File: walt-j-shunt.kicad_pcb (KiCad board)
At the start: 2 copper layers, 39 parts, among them Q1 NMOS, Q2 PNP, Q3 PNP

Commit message: basic layout positive
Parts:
- C1, C2: footprint Capacitor_THT:CP_Radial_D18.0mm_P7.50mm -> Capacitor_THT:CP_Radial_D12.5mm_P5.00mm
- C3: footprint Capacitor_THT:CP_Radial_D18.0mm_P7.50mm -> Samacsys:B32529C105J
- C4: footprint Capacitor_THT:CP_Radial_D5.0mm_P2.00mm -> Capacitor_SMD:C_0805_2012Metric
- D1, D2, D3, D4: footprint Diode_SMD:D_SMC -> Diode_SMD:D_SOD-123
- D6, D7: footprint Diode_SMD:D_SMC -> Diode_SMD:D_SOD-123F
- Q1: footprint Package_TO_SOT_THT:TO-3P-3_Horizontal_TabDown -> Package_TO_SOT_THT:TO-220-3_Horizontal_TabDown
- Q2: footprint Package_TO_SOT_THT:TO-3P-3_Horizontal_TabDown -> Package_TO_SOT_SMD:TO-252-2
- Q3: footprint Package_TO_SOT_THT:TO-3P-3_Horizontal_TabDown -> Package_TO_SOT_SMD:SOT-23-3
- R10, R9: footprint Resistor_SMD:R_1206_3216Metric -> Resistor_SMD:R_MELF_MMB-0207
- U1: value ~ -> AD817; footprint Package_SO:SOIC-8-1EP_3.9x4.9mm_P1.27mm_EP2.41x3.3mm -> Package_SO:SOIC-8_3.9x4.9mm_P1.27mm
- V1: value VSIN -> VPULSE
- moved H2 79.3 mm to (52.5, 90.0)
- moved H1 77.8 mm to (50.0, 52.5)
- moved V1 63.8 mm to (78.2, 70.5), turned to 90 degrees
- moved H3 57.8 mm to (170.0, 32.5)
- moved R1 53.9 mm to (88.0, 70.0), turned to 180 degrees
- moved D1 44.2 mm to (80.0, 79.0), turned to 180 degrees
- moved R2 43.6 mm to (99.0, 72.0), turned to 90 degrees
- moved R3 43.2 mm to (107.0, 61.0)
- moved R4 42.7 mm to (107.0, 65.0)
- moved D9 41.6 mm to (122.0, 64.7), turned to -90 degrees
- moved D2 40.0 mm to (80.0, 76.0)
- moved C1 39.8 mm to (92.0, 75.7), turned to -90 degrees
- moved D3 39.6 mm to (80.0, 82.0), turned to 180 degrees
- moved D4 38.8 mm to (80.0, 85.0)
- moved H4 36.1 mm to (160.0, 95.0)
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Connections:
- net Net-(Q1-D) renamed pre-cur
- U1 pad 1: Net-(D6-A) -> unconnected-(U1-NULL-Pad1)
- U1 pad 3: out -> Net-(D6-A)
- U1 pad 5: Net-(D5-K) -> unconnected-(U1-NC-Pad5)
- U1 pad 6: (no net) -> Net-(D5-K)
- U1 pad 7: (no net) -> out
- U1 pad 8: (no net) -> unconnected-(U1-NULL-Pad8)
- V1 pad 1: Net-(D1-A) -> ac
- V1 pad 2: ac -> Net-(D1-A)
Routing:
- net out: track 0.00 -> 106.4 mm
- net Net-(D6-A): track 0.00 -> 26.0 mm
- net Net-(D6-K): track 0.00 -> 25.7 mm
- net Net-(U1--): track 0.00 -> 16.9 mm
- net vref: track 0.00 -> 14.0 mm
- net Net-(D5-K): track 0.00 -> 13.0 mm
- net Net-(Q2-B): track 0.00 -> 12.7 mm
- net Net-(Q2-E): track 0.00 -> 12.3 mm
- net Net-(D5-A): track 0.00 -> 7.67 mm
- net Net-(D8-K): track 0.00 -> 4.80 mm

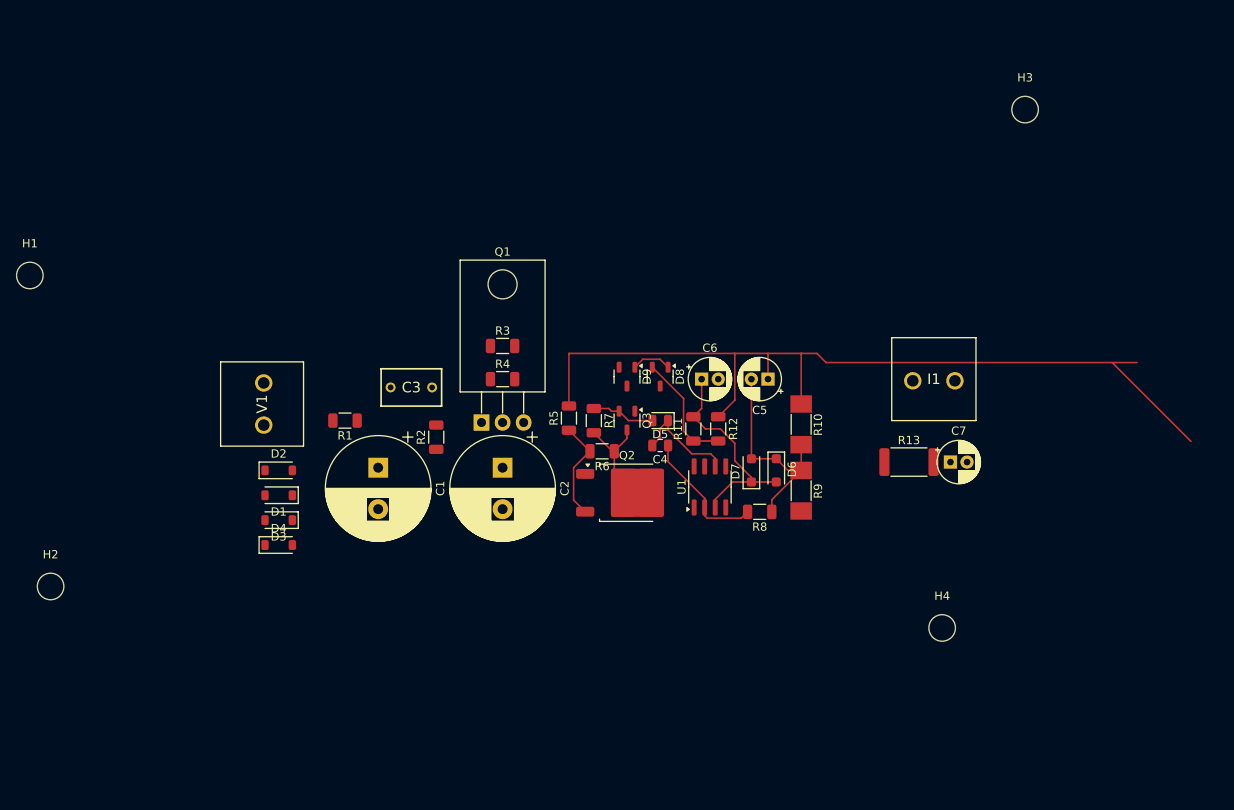
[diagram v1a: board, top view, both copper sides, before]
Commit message: plus only, cap and rectififer on board
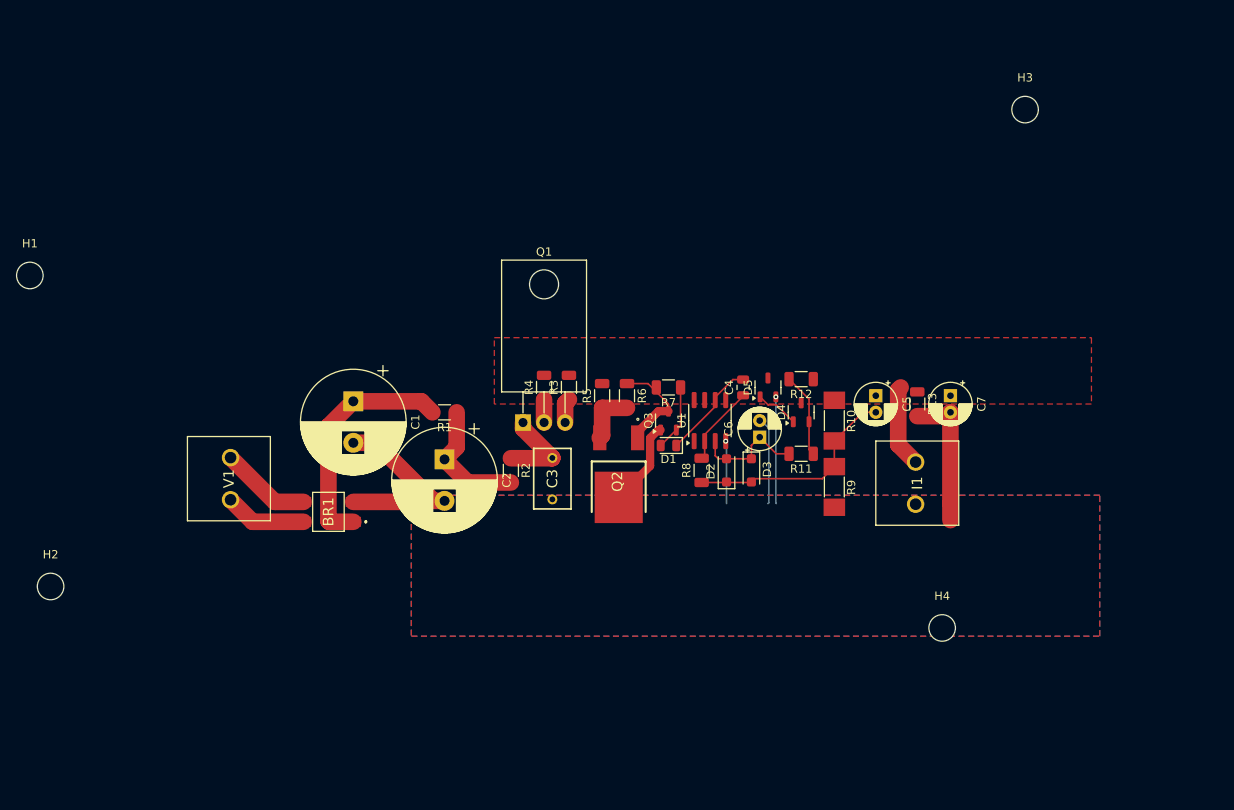
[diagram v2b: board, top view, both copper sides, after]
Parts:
- removed the D1 at (80.0, 79.0)
- removed the D2 at (80.0, 76.0)
- removed the D3 at (80.0, 82.0)
- removed the D4 at (80.0, 85.0)
- added BR1: CDBHM140L-G, Samacsys:CDBHM140LG, F.Cu at (86.0, 81.0)
- Q2: value PNP -> NJVMJD45H11T4G; footprint Package_TO_SOT_SMD:TO-252-2 -> Samacsys:DPAK_(SINGLE-GAUGE)_TO-252(369C)_ISSUE_F
- R13: footprint Resistor_SMD:R_2512_6332Metric -> Resistor_SMD:R_1206_3216Metric
- moved C3 21.3 mm to (113.0, 74.5), turned to -90 degrees
- moved D4 17.5 mm to (143.0, 69.0), turned to 90 degrees
- moved D5 17.0 mm to (139.0, 66.0), turned to 90 degrees
- moved R11 13.3 mm to (143.0, 74.0), turned to 180 degrees
- moved C5 13.2 mm to (152.0, 67.0), turned to -90 degrees
- moved C4 12.2 mm to (136.0, 66.0), turned to 90 degrees
- moved R1 12.0 mm to (100.0, 69.0)
- moved R12 11.7 mm to (143.0, 65.0), turned to 180 degrees
- moved C6 9.90 mm to (138.0, 72.0), turned to 90 degrees
- moved R2 9.85 mm to (108.0, 76.0), turned to -90 degrees
- moved R7 9.85 mm to (127.0, 66.0), turned to 180 degrees
- moved V1 9.85 mm to (74.2, 79.5)
- moved I1 9.81 mm to (156.8, 75.0), turned to -90 degrees
- moved R3 9.43 mm to (115.0, 66.0), turned to 90 degrees
- moved R8 8.60 mm to (131.0, 76.0), turned to 90 degrees
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- renumbered D5 to D1, D6 to D2, D7 to D3, D8 to D4, D9 to D5
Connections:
- Q2 pad 1: GND -> Net-(Q3-E)
- Q2 pad 2: Net-(Q2-B) -> Net-(Q2-Pad2)
- Q2 pad 3: Net-(Q2-E) -> GND
- Q3 pad 3: Net-(Q2-B) -> Net-(Q3-E)
- R5 pad 1: Net-(Q2-E) -> Net-(Q2-Pad2)
- R6 pad 1: Net-(Q2-B) -> Net-(Q3-E)
- R6 pad 2: Net-(Q2-E) -> Net-(Q2-Pad2)
- R7 pad 2: Net-(Q2-B) -> Net-(Q3-E)
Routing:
- net out: track 106.4 -> 9.99 mm
- net GND: track 0.00 -> 83.5 mm, vias 0 -> 2
- net Net-(BR1-+): track 0.00 -> 28.8 mm
- net Net-(C2-Pad1): track 0.00 -> 15.4 mm
- net Net-(Q2-B): track 12.7 -> 0.00 mm
- net Net-(Q3-E): track 0.00 -> 12.3 mm
- net Net-(Q2-E): track 12.3 -> 0.00 mm
- net Net-(D2-A): track 26.0 -> 13.8 mm
- net Net-(BR1-~{_2}): track 0.00 -> 11.0 mm
- net pre-cur: track 0.00 -> 10.8 mm
- net ac: track 0.00 -> 9.90 mm
- net Net-(U1--): track 16.9 -> 8.86 mm
- net Net-(Q2-Pad2): track 0.00 -> 6.73 mm
- net vref: track 14.0 -> 10.0 mm
- net Net-(Q1-S): track 0.00 -> 2.96 mm
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- added copper zone on B.Cu, net GND
- added copper zone on F.Cu, net GND
- added copper zone on F.Cu, net out

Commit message: working in subsheet
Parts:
- removed BR1: CDBHM140L-G, Samacsys:CDBHM140LG
- removed the C2 at (100.0, 74.7)
- removed the R1 at (100.0, 69.0)
- added C10: 120u, Capacitor_THT:CP_Radial_D5.0mm_P2.00mm, F.Cu at (171.0, 39.2)
- added C7: 33pf, Capacitor_SMD:C_0805_2012Metric, F.Cu at (191.2, 24.3)
- added C8: 120u, Capacitor_THT:CP_Radial_D5.0mm_P2.00mm, F.Cu at (171.0, 26.1)
- added C9: 120u, Capacitor_THT:CP_Radial_D5.0mm_P2.00mm, F.Cu at (171.0, 32.6)
- added D10: D_Zener, Diode_SMD:D_MiniMELF, F.Cu at (171.8, 47.5)
- added D6: LED, Diode_SMD:D_0805_2012Metric, F.Cu at (191.2, 27.3)
- added D7: D, Diode_SMD:D_SOD-123F, F.Cu at (191.3, 32.2)
- added D8: D, Diode_SMD:D_SOD-123F, F.Cu at (191.3, 35.6)
- added D9: D_Zener, Diode_SMD:D_MiniMELF, F.Cu at (171.8, 44.1)
- added I2: 20ma, Samacsys:395443002, F.Cu at (179.3, 37.3)
- added Q4: NJVMJD45H11T4G, Samacsys:DPAK_(SINGLE-GAUGE)_TO-252(369C)_ISSUE_F, F.Cu at (177.1, 26.7)
- added Q5: PNP, Package_TO_SOT_SMD:SOT-23-3, F.Cu at (191.1, 39.6)
- added R12: 1r, Resistor_SMD:R_1206_3216Metric, F.Cu at (165.8, 24.4)
- added R14: 221r, Resistor_SMD:R_1206_3216Metric, F.Cu at (165.8, 31.0)
- added R15: 499, Resistor_SMD:R_1206_3216Metric, F.Cu at (165.8, 34.3)
- added R16: 1k, Resistor_SMD:R_MELF_MMB-0207, F.Cu at (179.5, 45.7)
- added R17: 800r, Resistor_SMD:R_MELF_MMB-0207, F.Cu at (179.5, 49.9)
- added R18: 1k, Resistor_SMD:R_1206_3216Metric, F.Cu at (165.8, 37.6)
- added R19: 1.82k, Resistor_SMD:R_1206_3216Metric, F.Cu at (165.8, 40.9)
- added U2: AD817, Package_SO:SOIC-8_3.9x4.9mm_P1.27mm, F.Cu at (188.0, 47.0)
- C1: value 2200uf -> 120u; footprint Capacitor_THT:CP_Radial_D12.5mm_P5.00mm -> Capacitor_THT:CP_Radial_D5.0mm_P2.00mm
- D4, D5: footprint Package_TO_SOT_SMD:SOT-23-3 -> Diode_SMD:D_MiniMELF
- R13: value 1k -> 49.9r
- V1: value VPULSE -> VSIN
- moved R13 41.2 mm to (165.8, 27.7), turned to 0 degrees
- moved H3 31.5 mm to (159.8, 62.2)
- moved V1 25.4 mm to (99.0, 74.5), turned to -90 degrees
- moved C1 22.1 mm to (108.0, 79.0)
- moved D5 8.49 mm to (145.2, 71.8)
- moved R7 7.82 mm to (138.8, 76.1), turned to 180 degrees
- moved R10 6.64 mm to (140.8, 67.8)
- moved R9 6.43 mm to (148.5, 76.2), turned to 180 degrees
- moved C3 6.37 mm to (131.2, 70.2), turned to 180 degrees
- moved C6 5.50 mm to (155.5, 67.0)
- moved D2 5.37 mm to (138.8, 73.6), turned to 180 degrees
- moved D3 5.19 mm to (138.8, 71.1), turned to 0 degrees
- moved C5 4.84 mm to (136.2, 67.5), turned to 180 degrees
- moved C4 4.68 mm to (150.7, 71.5), turned to 180 degrees
- moved U1 4.22 mm to (132.8, 74.1), turned to 180 degrees
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- renumbered C3 to C2, C4 to C3, C5 to C4, C6 to C5, C7 to C6, R2 to R1, R11 to R10, R12 to R11, R3 to R2, R4 to R3, R5 to R4, R6 to R5, R7 to R6, R8 to R7, R9 to R8, R10 to R9
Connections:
- C1 pad 1: Net-(BR1-+) -> bank-plus
- R1 pad 2: Net-(C2-Pad1) -> bank-plus
- R13 pad 1: out -> Net-(Q5-E)
- R13 pad 2: GND -> Net-(Q4-Pad2)
- V1 pad 1: ac -> bank-plus
- V1 pad 2: Net-(BR1-~{_2}) -> GND
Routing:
- net Net-(BR1-+): track 28.8 -> 0.00 mm
- net GND: track 83.5 -> 55.4 mm, vias 2 -> 30
- net out: track 9.99 -> 26.3 mm, vias 0 -> 2
- net Net-(C2-Pad1): track 15.4 -> 0.00 mm
- net bank-plus: track 0.00 -> 12.0 mm
- net Net-(BR1-~{_2}): track 11.0 -> 0.00 mm
- net ac: track 9.90 -> 0.00 mm
- net Net-(D2-K): track 26.3 -> 17.2 mm
- net vref: track 10.0 -> 4.30 mm
- net Net-(D1-K): track 12.0 -> 7.37 mm
- net Net-(D4-K): track 5.24 -> 2.50 mm
- net Net-(D2-A): track 13.8 -> 12.1 mm
- net pre-cur: track 10.8 -> 11.8 mm

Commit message: bipolar. untested
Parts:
- added C11: 120u, Capacitor_THT:CP_Radial_D5.0mm_P2.00mm, F.Cu at (136.5, 85.3)
- added C12: 120u, Capacitor_THT:CP_Radial_D5.0mm_P2.00mm, F.Cu at (155.0, 95.0)
- added Q6: PNP, Package_TO_SOT_SMD:SOT-23-3, F.Cu at (127.2, 87.8)
- added R20: 800r, Resistor_SMD:R_MELF_MMB-0207, F.Cu at (148.8, 94.0)
- added R21: 1k, Resistor_SMD:R_1206_3216Metric, F.Cu at (141.0, 85.5)
- added R22: 1.82k, Resistor_SMD:R_1206_3216Metric, F.Cu at (145.8, 85.5)
- added V2: VSIN, Samacsys:395443002, F.Cu at (98.8, 82.5)
- C7: value 33pf -> 120u; footprint Capacitor_SMD:C_0805_2012Metric -> Capacitor_THT:CP_Radial_D5.0mm_P2.00mm
- C8: value 120u -> 1uf; footprint Capacitor_THT:CP_Radial_D5.0mm_P2.00mm -> Samacsys:B32529C105J
- C9: value 120u -> 33pf; footprint Capacitor_THT:CP_Radial_D5.0mm_P2.00mm -> Capacitor_SMD:C_0805_2012Metric
- Q4: value NJVMJD45H11T4G -> NMOS; footprint Samacsys:DPAK_(SINGLE-GAUGE)_TO-252(369C)_ISSUE_F -> Package_TO_SOT_THT:TO-220-3_Horizontal_TabDown
- Q5: value PNP -> NJVMJD45H11T4G; footprint Package_TO_SOT_SMD:SOT-23-3 -> Samacsys:DPAK_(SINGLE-GAUGE)_TO-252(369C)_ISSUE_F
- R13: value 49.9r -> 5r
- R14: value 221r -> 100r
- R15: value 499 -> 1r
- R16: value 1k -> 49.9r; footprint Resistor_SMD:R_MELF_MMB-0207 -> Resistor_SMD:R_1206_3216Metric
- R17: value 800r -> 221r; footprint Resistor_SMD:R_MELF_MMB-0207 -> Resistor_SMD:R_1206_3216Metric
- R18: value 1k -> 499
- R19: value 1.82k -> 1k; footprint Resistor_SMD:R_1206_3216Metric -> Resistor_SMD:R_MELF_MMB-0207
- moved C7 116.3 mm to (98.0, 94.0)
- moved Q4 107.0 mm to (110.0, 110.0), turned to 180 degrees
- moved R12 93.7 mm to (103.0, 94.0), turned to -90 degrees
- moved Q5 91.5 mm to (121.3, 98.8), turned to 90 degrees
- moved D6 90.2 mm to (127.5, 91.3), turned to 180 degrees
- moved R13 84.9 mm to (107.0, 89.0), turned to 90 degrees
- moved C8 82.3 mm to (112.5, 84.0), turned to 180 degrees
- moved R14 80.5 mm to (110.0, 89.0), turned to 90 degrees
- moved D7 78.9 mm to (139.1, 91.4), turned to 180 degrees
- moved D8 74.6 mm to (139.1, 88.9)
- moved U2 70.9 mm to (133.1, 91.9), turned to 180 degrees
- moved R16 69.3 mm to (122.2, 84.8), turned to -90 degrees
- moved R15 68.6 mm to (119.2, 84.8), turned to 90 degrees
- moved C9 68.0 mm to (131.5, 88.0), turned to 180 degrees
- moved R18 62.3 mm to (139.1, 93.9), turned to 180 degrees
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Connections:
- net out renamed pos_reg_out
- C10 pad 1: /reg/in_plus -> GND
- C10 pad 2: GND -> Net-(D7-K)
- C7 pad 1: Net-(U2--) -> GND
- C7 pad 2: Net-(D6-K) -> Net-(C7-Pad2)
- C8 pad 1: /reg/in_plus -> GND
- C8 pad 2: Net-(D7-K) -> /current_source1/plus
- C9 pad 1: Net-(D7-A) -> Net-(U2--)
- C9 pad 2: GND -> Net-(D6-K)
- D10 pad 2: GND -> neg_reg_out
- D4 pad 2: vref -> Net-(D4-A)
- D9 pad 2: vref -> Net-(D9-A)
- I2 pad 1: /reg/in_plus -> GND
- I2 pad 2: GND -> neg_reg_out
- Q4 pad 1: Net-(Q5-E) -> neg_reg_out
- Q4 pad 2: Net-(Q4-Pad2) -> Net-(Q4-G)
- Q4 pad 3: GND -> Net-(Q4-S)
- Q5 pad 1: GND -> Net-(Q6-E)
- Q5 pad 2: Net-(D6-A) -> Net-(Q5-Pad2)
- Q5 pad 3: Net-(Q5-E) -> neg_reg_out
- R10 pad 1: vref -> Net-(D4-A)
- R11 pad 2: vref -> Net-(D4-A)
- R12 pad 1: Net-(Q4-Pad2) -> /current_source1/plus
- R12 pad 2: /reg/in_plus -> Net-(C7-Pad2)
- R13 pad 1: Net-(Q5-E) -> Net-(Q4-S)
- R13 pad 2: Net-(Q4-Pad2) -> /current_source1/plus
- R14 pad 1: Net-(D6-A) -> Net-(Q4-G)
- R14 pad 2: Net-(Q5-E) -> /current_source1/plus
- R15 pad 1: Net-(D7-K) -> Net-(Q5-Pad2)
- R15 pad 2: Net-(U2--) -> GND
- R16 pad 1: Net-(D7-K) -> Net-(Q6-E)
- R16 pad 2: GND -> Net-(Q5-Pad2)
- R17 pad 1: /reg/in_plus -> Net-(D6-A)
- R17 pad 2: Net-(D7-K) -> Net-(Q6-E)
- R18 pad 1: vref -> Net-(D7-K)
- R18 pad 2: Net-(D7-A) -> Net-(U2--)
- R19 pad 1: /reg/in_plus -> Net-(D7-K)
- R19 pad 2: vref -> neg_reg_out
- U2 pad 4: GND -> neg_reg_out
- U2 pad 7: /reg/in_plus -> GND
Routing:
- net neg_reg_out: track 0.00 -> 61.8 mm, vias 0 -> 33
- net GND: track 55.4 -> 102.1 mm, vias 30 -> 37
- net /current_source1/plus: track 0.00 -> 19.2 mm
- net Net-(D7-K): track 0.00 -> 17.2 mm
- net Net-(Q6-E): track 0.00 -> 12.3 mm
- net Net-(D7-A): track 0.00 -> 12.1 mm
- net Net-(C7-Pad2): track 0.00 -> 10.6 mm
- net Net-(U2--): track 0.00 -> 9.25 mm
- net Net-(D6-A): track 0.00 -> 8.01 mm
- net Net-(D6-K): track 0.00 -> 7.37 mm
- net Net-(Q5-Pad2): track 0.00 -> 6.73 mm
- net vref: track 4.30 -> 0.00 mm
- net Net-(D9-A): track 0.00 -> 4.30 mm
- net Net-(D4-A): track 0.00 -> 4.30 mm
- net bank-plus: track 12.0 -> 16.1 mm
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- added copper zone on B.Cu, net neg_reg_out
- added copper zone on F.Cu, net neg_reg_out
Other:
- board outline added: 70 x 50 mm

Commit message: pretty neat neg needs testing
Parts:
- removed I1, I2: 20ma, Samacsys:395443002
- added J1: Screw_Terminal_01x03, TerminalBlock_Altech:Altech_AK100_1x03_P5.00mm, F.Cu at (156.7, 75.0)
- moved V1 2.24 mm to (100.8, 71.5)
- moved V2 2.07 mm to (100.8, 83.0)
- moved C1 2.00 mm to (110.0, 77.0)
- moved C2 2.00 mm to (109.0, 72.0)
- moved C8 2.00 mm to (114.5, 84.0)
- moved R1 2.00 mm to (114.0, 78.0)
- moved R13 1.00 mm to (108.0, 89.0)
- moved R14 1.00 mm to (111.0, 89.0)
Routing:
- net GND: track 102.1 -> 121.6 mm, vias 37 -> 60
- net neg_reg_out: track 61.8 -> 76.6 mm, vias 33 -> 55
- net pos_reg_out: track 29.0 -> 32.1 mm
- net /current_source1/plus: track 19.2 -> 20.0 mm
- net Net-(C7-Pad2): track 10.6 -> 9.86 mm
- added copper zone on B.Cu, net pos_reg_out
